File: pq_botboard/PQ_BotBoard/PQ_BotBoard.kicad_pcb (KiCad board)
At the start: 6 copper layers, 64 x 52 mm, 31 parts, among them IC1 TCN75AVOA713, J1 53261-1471, J2 Conn_01x08_MountingPin, J3 53261-0271

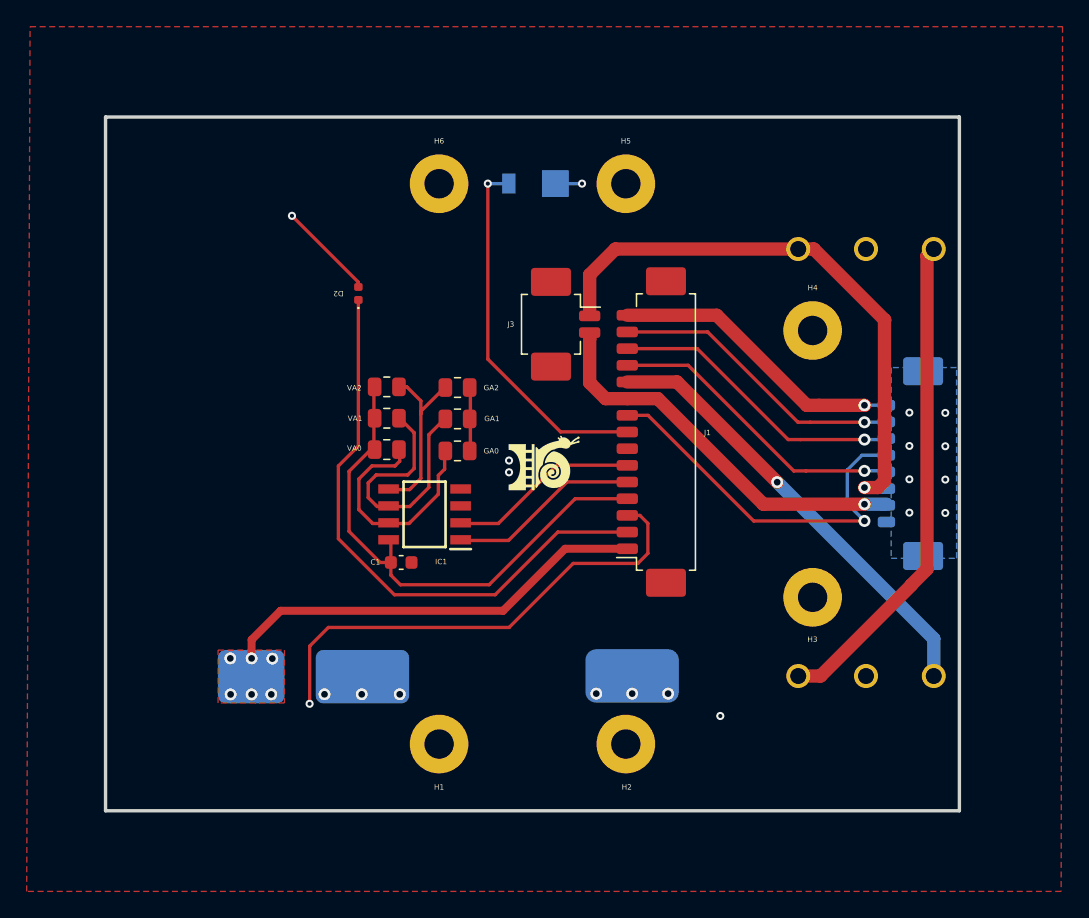
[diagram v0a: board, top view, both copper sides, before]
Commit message: Added a charging protection for the battery using the umbilical (antireturn Schottky diode and LDO) and regenerated the production files
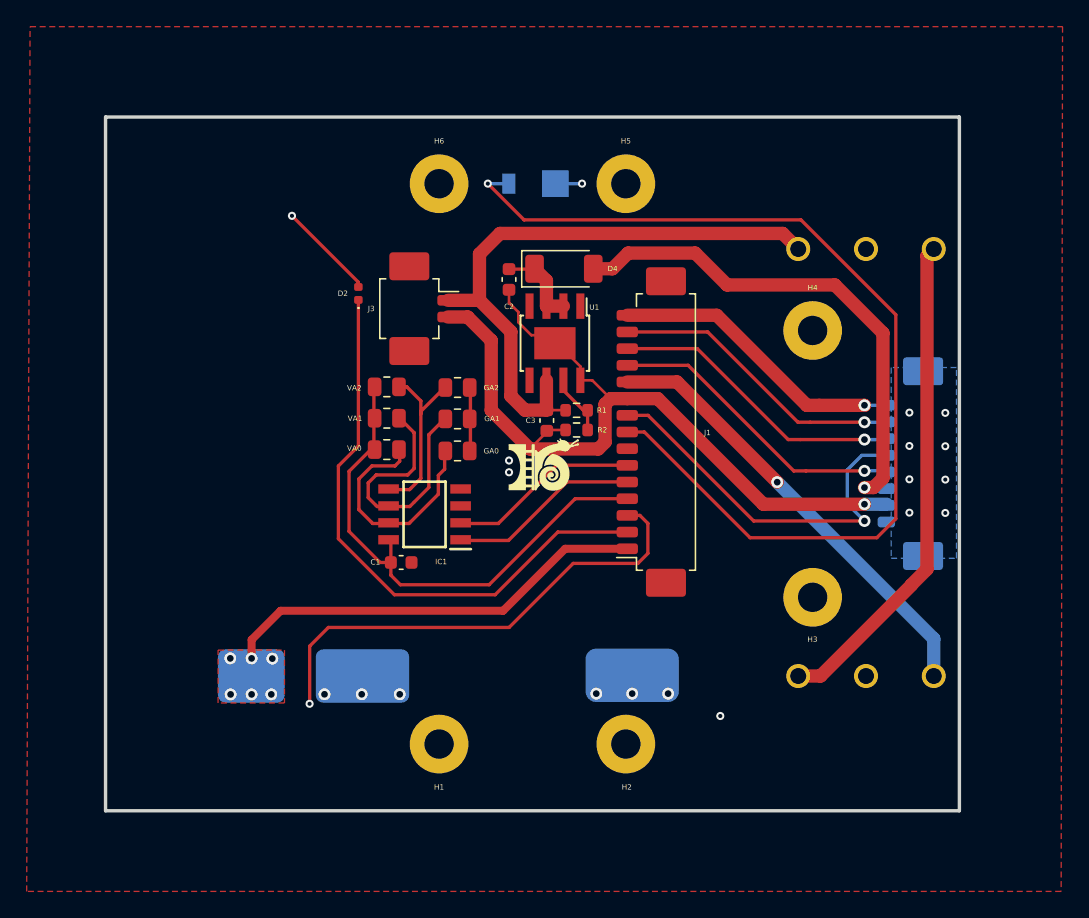
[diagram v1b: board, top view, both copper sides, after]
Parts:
- added C2: 10uF, Capacitor_SMD:C_0603_1608Metric, F.Cu at (100.2, 43.2)
- added C3: 10uF, Capacitor_SMD:C_0603_1608Metric, F.Cu at (103.1, 53.7)
- added D4: ~, passive-nsl:RBS1LAM40ATR_Schottky, F.Cu at (104.4, 42.4)
- added R1: 224k, Resistor_SMD:R_0603_1608Metric, F.Cu at (105.3, 53.0)
- added R2: 33k, Resistor_SMD:R_0603_1608Metric, F.Cu at (105.3, 54.5)
- added U1: TPS7A7002DDAR, Package_SO:TI_SO-PowerPAD-8, F.Cu at (103.7, 48.0)
- moved J3 10.7 mm to (93.3, 45.4)
- moved Annotation6 0.21 mm to (103.4, 57.8)
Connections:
- J2 pad 6: /BATT+ -> /CHARGE+
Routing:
- net /PH+: track 27.5 -> 75.5 mm
- net /CHARGE+: track 0.00 -> 38.9 mm, vias 0 -> 1
- net /BATT-: track 29.3 -> 60.4 mm
- net Net-(U1-EN): track 0.00 -> 6.37 mm
- net Net-(U1-FB): track 0.00 -> 4.66 mm
- net /BATT+: track 43.2 -> 45.8 mm, vias 1 -> 0

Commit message: Recenter components to fit inside the square hole of the slider, change PicoBlade from 2 pins to 3 pins
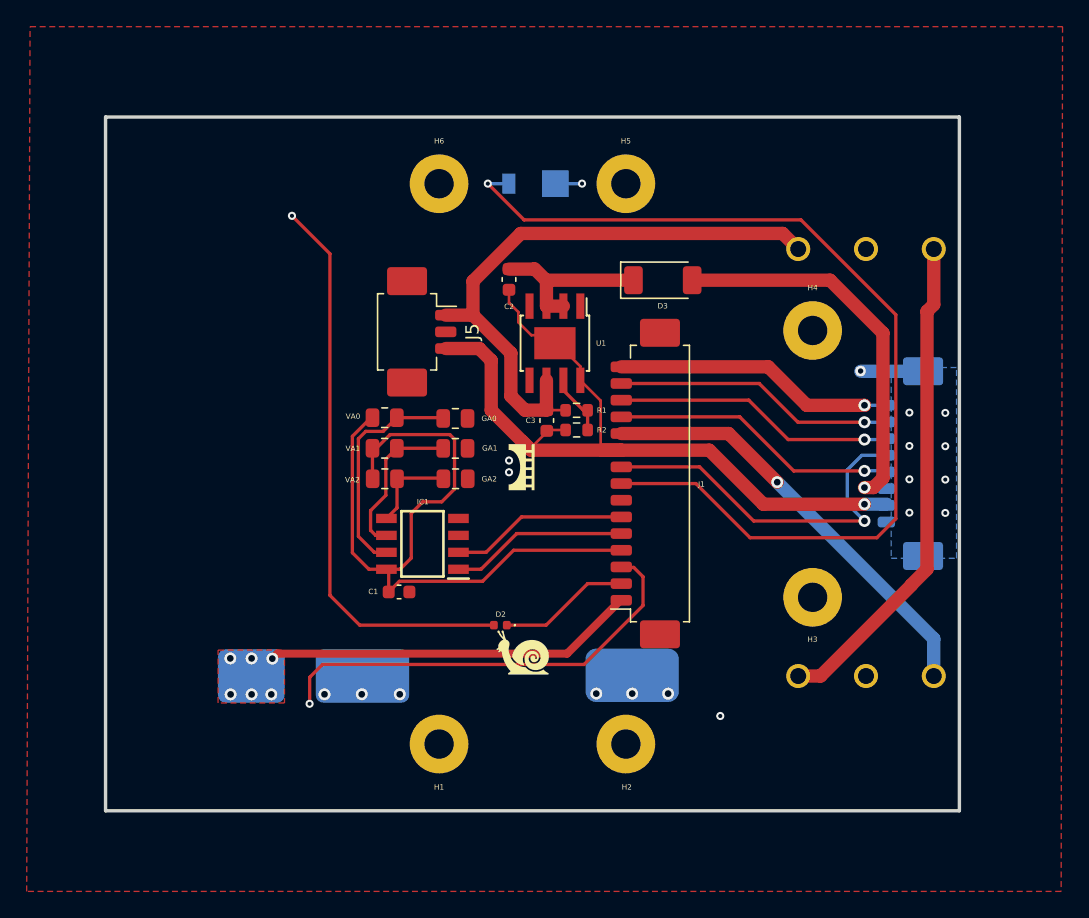
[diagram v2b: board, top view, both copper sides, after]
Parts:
- removed J3: 53261-0271, Connector_Molex:Molex_PicoBlade_53261-0271_1x02-1MP_P1.25mm_Horizontal
- added J5: Conn_01x03_MountingPin, Connector_Molex:Molex_PicoBlade_53261-0371_1x03-1MP_P1.25mm_Horizontal, F.Cu at (93.1, 47.1)
- R1: value 224k -> 340k
- R2: value 33k -> 50k
- moved D2 27.0 mm to (99.6, 69.1), turned to 180 degrees
- moved Annotation6 13.9 mm to (102.0, 71.6), turned to 0 degrees
- moved D3 7.46 mm to (111.8, 43.2)
- moved VA2 6.89 mm to (90.9, 58.1)
- moved GA2 6.84 mm to (96.2, 58.1)
- moved J1 3.89 mm to (111.1, 58.5)
- moved GA0 2.44 mm to (96.2, 53.6)
- moved VA0 2.40 mm to (90.9, 53.5)
- moved VA1 2.26 mm to (90.9, 55.8)
- moved IC1 2.22 mm to (93.8, 63.0)
- moved C1 2.22 mm to (92.0, 66.6)
- moved GA1 2.22 mm to (96.2, 55.8)
- renumbered D4 to D3
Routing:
- net /MAG-Y: track 43.9 -> 9.87 mm
- net /VCC_MAG: track 9687.4 -> 9719.6 mm
- net /VCC: track 39.1 -> 56.7 mm
- net /CHARGE+: track 38.9 -> 30.2 mm
- net Net-(IC1-A1): track 20.1 -> 11.8 mm
- net Net-(U1-EN): track 6.37 -> 12.9 mm
- net Net-(IC1-A2): track 13.2 -> 6.78 mm
- net /SOLAR_Y: track 32.4 -> 28.0 mm
- net GND: track 7.09 -> 8.74 mm, vias 15 -> 16
- net /SCL: track 14.6 -> 13.3 mm
- net /SDA: track 14.6 -> 13.3 mm
- net /BATT-: track 60.4 -> 59.3 mm
- net /SWDIO: track 22.2 -> 21.1 mm
- net /PH+: track 75.5 -> 74.4 mm
- net /KILLSWITCH+: track 33.7 -> 32.6 mm
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
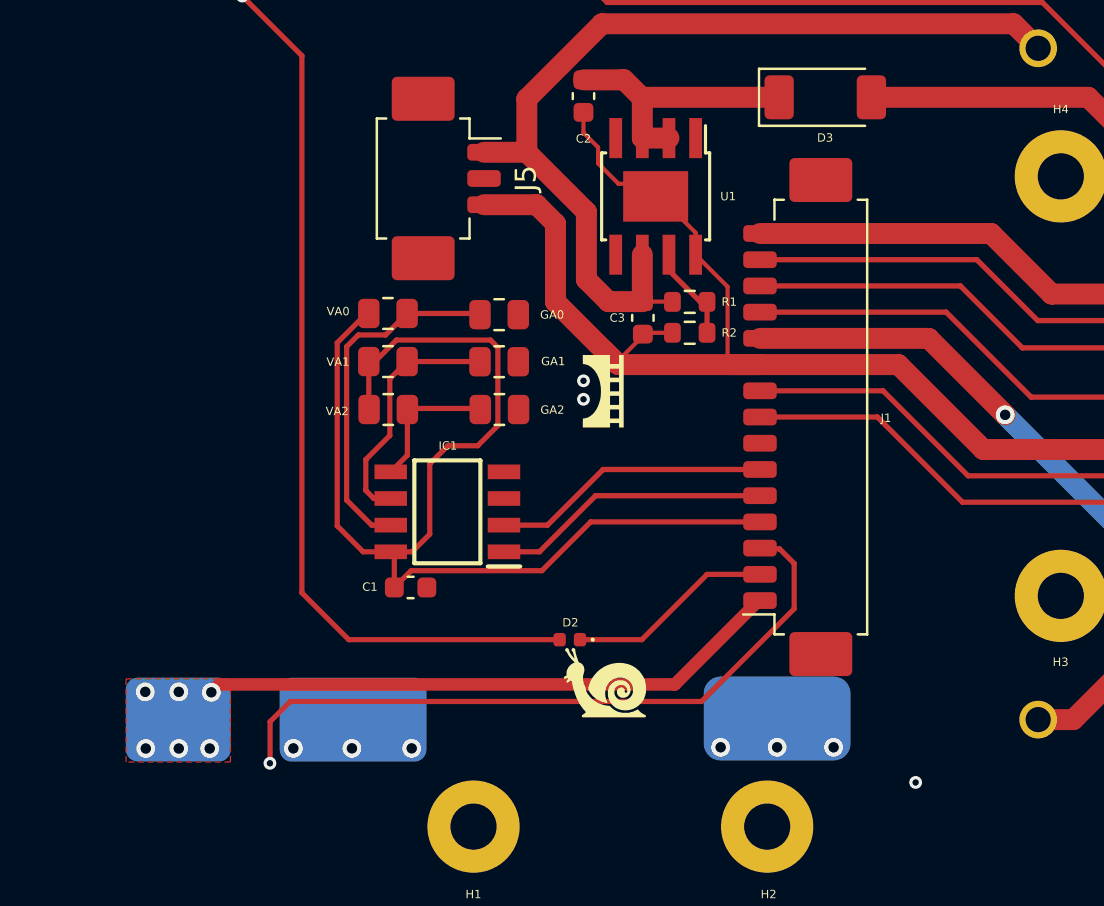
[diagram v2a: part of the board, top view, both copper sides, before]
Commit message: add Lighticity SC to bottom with the option to solder using epoxy
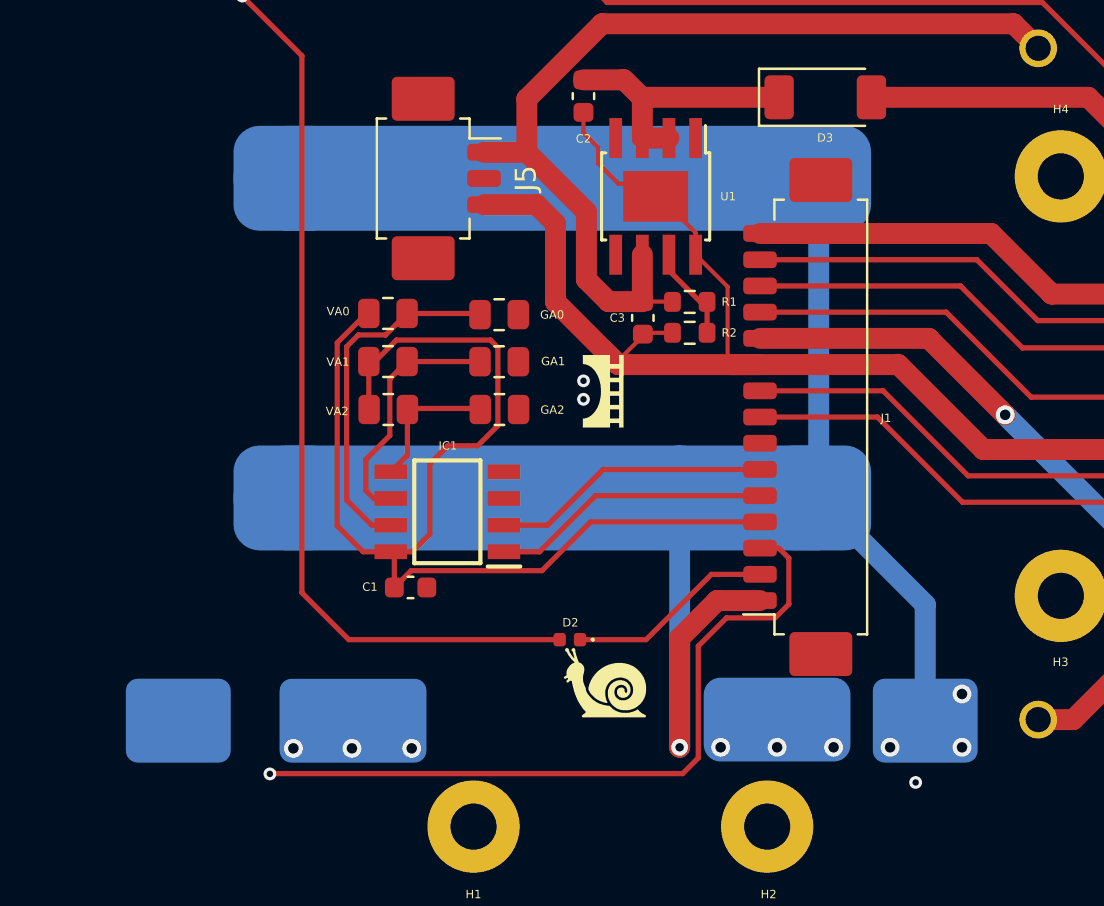
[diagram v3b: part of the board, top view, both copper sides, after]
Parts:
- removed SC1: ~, power-nsl:Lighttricity_S3040_CIC
- added SC2: ~, power-nsl:Lighttricity_S3040_CIC, B.Cu at (78.4, 70.0)
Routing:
- net /SOLAR_Y: track 28.0 -> 100.4 mm, vias 6 -> 4
- net /VCC_MAG: track 9719.6 -> 9721.8 mm
- removed copper zone on F.Cu, net /SOLAR_Y
